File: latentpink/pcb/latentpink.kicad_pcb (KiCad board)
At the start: 8 copper layers, 145 x 139 mm, 829 parts, among them J1 CONN_SFP_HOST, J10 XILINX_JTAG, J11 FAN_01, J12 FAN_01, J13 CONN_01X05, J14 CONN_01X03, J15 CONN_01X03, J16 JUMPER_0402_SPDT, J17 JUMPER_0402_SPDT, J18 BEL_FUSE_0845-2R1T-E4, J19 BEL_FUSE_0845-2R1T-E4, J2 SFP_CAGE, J20 BEL_FUSE_0845-2R1T-E4, J21 BEL_FUSE_0845-2R1T-E4, J22 BEL_FUSE_0845-2R1T-E4, J23 PMOD_HOST, J3 XILINX_JTAG, J4 BEL_FUSE_0845-2R1T-E4, J5 0826-1G1T-23-F, J6 BARREL_JACK, J7 RJ45, J8 BEL_FUSE_0845-2R1T-E4, J9 XILINX_JTAG, M1 960-27-12-D-AB-0, M10 WEEE, M2 960-23-23-F-AB-0, M3 SCREWHOLE, M4 SCREWHOLE, M5 SCREWHOLE, M6 SCREWHOLE, M7 LONGTHING, M8 OSHW, M9 POLARITY, U1 VSC8512, U10 MYMGK1R812ERSR, U11 MYMGK00504ERSR, U12 STM32L031-QFN32, U13 MYMGK00504ERSR, U14 MYMGK00504ERSR, U15 MYMGK00504ERSR, U16 NCP45521IMNTWG-H, U17 NCP45521IMNTWG-H, U18 LP2996AMRE, U19 TPS7A2533DRVR, U2 XC7K160T-2FBG484C, U20 AT24MAC402, U21 ECX2-LMV-3CN-125.000-TR, U22 ECS-2016MVQ-250-CN, U23 ADM3101E_QFN, U24 SIT9121AI-2BF-XXS200.000000G, U25 SIT9121AI-2BF-XXS156.250000G, U26 74LVC1T45, U27 74LVC1T45, U28 IS25WP256D-JLLE, U29 DSC1123CI2-150.0000T, U3 CY7C2245KV18-450BZXI, U30 DSC1123CI2-150.0000T, U31 74LVC1T45, U32 74LVC1T45, U33 74LVC1T45, U34 74LVC1T45, U35 SIT9121AC-2B2-33E125.000000, U36 AT30TS74_UDFN, U37 AT30TS74_UDFN, U38 AT30TS74_UDFN, U39 AT30TS74_UDFN, U4 STM32H735-UFBGA176-25, U40 RCLAMP0514M, U41 RCLAMP0514M, U42 RCLAMP0514M, U43 RCLAMP0514M, U44 RCLAMP0514M, U45 RCLAMP0514M, U46 RCLAMP0514M, U47 RCLAMP0514M, U48 RCLAMP0514M, U49 RCLAMP0514M, U5 DP83867, U50 RCLAMP0514M, U51 RCLAMP0514M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

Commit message: Continued initial layout. Working on PHY decoupling caps and fanout
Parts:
- C1, C112, C264, C266, C267, C268, C270, C271, C272, C273, C274, C275, C277, C279, C280, C281, C282, C283, C286, C287, C290, C291, C294, C301, C302, C303, C308, C329, C333, C336, C337, C346, C347, C350, C351, C475, C67, C70, L4, R20, R21, R80: moved to B.Cu
- moved C100 182.3 mm to (136.0, 145.5)
- moved C107 176.0 mm to (127.8, 135.8), turned to 180 degrees
- moved C475 172.5 mm to (132.5, 138.5)
- moved C103 170.9 mm to (120.8, 145.5), turned to 180 degrees
- moved TP3 169.2 mm to (122.5, 142.0)
- moved R8 169.1 mm to (133.0, 142.0)
- moved R11 167.9 mm to (134.2, 142.5), turned to 90 degrees
- moved C112 162.2 mm to (127.8, 138.5), turned to 180 degrees
- moved TP20 147.3 mm to (111.0, 74.2)
- moved TP19 145.5 mm to (112.5, 74.2)
- moved R20 115.6 mm to (124.8, 142.0), turned to 180 degrees
- moved R21 115.5 mm to (126.0, 143.2)
- moved R36 114.3 mm to (132.5, 139.8), turned to 90 degrees
- moved C279 104.5 mm to (125.5, 89.2), turned to -90 degrees
- moved C303 104.2 mm to (117.0, 83.8)
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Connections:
- R100 pad 1: /QSGMII PHY/PHY7_LED1_N -> /QSGMII PHY/PHY6_LED1_N
- R81 pad 1: /QSGMII PHY/PHY0_LED0_N -> /QSGMII PHY/PHY1_LED0_N
- R82 pad 1: /QSGMII PHY/PHY1_LED0_N -> /QSGMII PHY/PHY0_LED0_N
- R83 pad 1: /QSGMII PHY/PHY2_LED0_N -> /QSGMII PHY/PHY3_LED0_N
- R84 pad 1: /QSGMII PHY/PHY3_LED0_N -> /QSGMII PHY/PHY2_LED0_N
- R85 pad 1: /QSGMII PHY/PHY4_LED0_N -> /QSGMII PHY/PHY5_LED0_N
- R86 pad 1: /QSGMII PHY/PHY5_LED0_N -> /QSGMII PHY/PHY4_LED0_N
- R87 pad 1: /QSGMII PHY/PHY6_LED0_N -> /QSGMII PHY/PHY7_LED0_N
- R88 pad 1: /QSGMII PHY/PHY7_LED0_N -> /QSGMII PHY/PHY6_LED0_N
- R93 pad 1: /QSGMII PHY/PHY0_LED1_N -> /QSGMII PHY/PHY1_LED1_N
- R94 pad 1: /QSGMII PHY/PHY1_LED1_N -> /QSGMII PHY/PHY0_LED1_N
- R95 pad 1: /QSGMII PHY/PHY2_LED1_N -> /QSGMII PHY/PHY3_LED1_N
- R96 pad 1: /QSGMII PHY/PHY3_LED1_N -> /QSGMII PHY/PHY2_LED1_N
- R97 pad 1: /QSGMII PHY/PHY4_LED1_N -> /QSGMII PHY/PHY5_LED1_N
- R98 pad 1: /QSGMII PHY/PHY5_LED1_N -> /QSGMII PHY/PHY4_LED1_N
- R99 pad 1: /QSGMII PHY/PHY6_LED1_N -> /QSGMII PHY/PHY7_LED1_N
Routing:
- net /GND: track 717.2 -> 865.2 mm, vias 253 -> 340
- net /12V0: track 0.00 -> 81.3 mm, vias 0 -> 10
- net /2V5: track 162.5 -> 208.7 mm, vias 37 -> 61
- net /QSGMII PHY/QSGMII Power/A2V5_VSC: track 53.7 -> 77.2 mm, vias 36 -> 46
- net /QSGMII PHY/QSGMII Power/A1V0_VSC: track 40.1 -> 60.6 mm, vias 24 -> 45
- net /QSGMII PHY/VSC_JTAG_TDO: track 60.6 -> 77.0 mm
- net /Power Supply/2V5_RAW: track 0.00 -> 7.21 mm, vias 0 -> 6
- net /QSGMII PHY/VSC_JTAG_TDI: track 60.3 -> 67.3 mm
- net /1V0: track 88.0 -> 94.7 mm, vias 81 -> 84
- net /QSGMII PHY/VSC_JTAG_TCK: track 67.8 -> 74.2 mm
- net /QSGMII PHY/VSC_CLKOUT_1: track 0.00 -> 6.21 mm
- net Net-(U1-PadW4): track 0.00 -> 5.46 mm, vias 0 -> 2
- net Net-(U1-PadV4): track 0.00 -> 5.46 mm, vias 0 -> 1
- net Net-(U1-PadT4): track 0.00 -> 5.46 mm, vias 0 -> 2
- net /QSGMII PHY/VSC_CLKOUT_0: track 0.00 -> 5.41 mm
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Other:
- board text added: "2V5_PGOOD"
- board text added: "A2V5_VSC"
- board text added: "CLKOUT0"
- board text added: "CLKOUT1"

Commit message: Lots of layout progress on bottom power/management/supervisor area
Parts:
- C110, C115, C116, C119, C121, C13, C20, C262, C284, C289, C292, C293, C313, C318, C323, C325, C331, C352, C353, C354, C466, C6, L2, L5, R106, R107, R109, R110, R111, R12, R23, R9: moved to B.Cu
- moved TP6 180.4 mm to (111.5, 25.0)
- moved C113 169.6 mm to (117.8, 132.5), turned to 90 degrees
- moved C104 169.3 mm to (118.5, 138.8), turned to -90 degrees
- moved C468 161.4 mm to (105.8, 83.3), turned to -90 degrees
- moved C467 159.7 mm to (104.8, 83.2), turned to -90 degrees
- moved U35 157.0 mm to (105.8, 80.2), turned to 180 degrees
- moved C101 156.6 mm to (115.0, 138.8), turned to 90 degrees
- moved C466 151.7 mm to (107.2, 81.2)
- moved C476 150.7 mm to (121.0, 132.5), turned to 90 degrees
- moved R9 148.6 mm to (112.5, 138.0), turned to -90 degrees
- moved C108 147.5 mm to (114.5, 132.5), turned to 90 degrees
- moved R12 146.1 mm to (112.5, 139.8), turned to 90 degrees
- moved C117 127.1 mm to (70.2, 138.0), turned to 90 degrees
- moved R109 125.1 mm to (127.0, 80.8), turned to -90 degrees
- moved D10 123.1 mm to (92.5, 141.0), turned to 180 degrees
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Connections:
- R100 pad 1: /QSGMII PHY/PHY6_LED1_N -> /QSGMII PHY/PHY7_LED1_N
- R100 pad 2: Net-(U1-PadW4) -> Net-(R100-Pad2)
- R101 pad 2: Net-(U1-PadW3) -> Net-(R101-Pad2)
- R102 pad 2: Net-(U1-PadW2) -> Net-(R102-Pad2)
- R103 pad 2: Net-(U1-PadW1) -> Net-(R103-Pad2)
- R104 pad 2: Net-(U1-PadV4) -> Net-(R104-Pad2)
- R106 pad 1: /QSGMII PHY/VSC_RST_N -> /2V5
- R106 pad 2: /2V5 -> /QSGMII PHY/VSC_RST_N
- R81 pad 1: /QSGMII PHY/PHY1_LED0_N -> /QSGMII PHY/PHY0_LED0_N
- R81 pad 2: Net-(U1-PadV3) -> Net-(U1-PadV2)
- R82 pad 1: /QSGMII PHY/PHY0_LED0_N -> /QSGMII PHY/PHY1_LED0_N
- R82 pad 2: Net-(U1-PadV2) -> Net-(U1-PadV3)
- R83 pad 1: /QSGMII PHY/PHY3_LED0_N -> /QSGMII PHY/PHY2_LED0_N
- R83 pad 2: Net-(U1-PadV1) -> Net-(R83-Pad2)
- R84 pad 1: /QSGMII PHY/PHY2_LED0_N -> /QSGMII PHY/PHY3_LED0_N
- R84 pad 2: Net-(U1-PadU4) -> Net-(R84-Pad2)
- R85 pad 1: /QSGMII PHY/PHY5_LED0_N -> /QSGMII PHY/PHY4_LED0_N
- R85 pad 2: Net-(U1-PadU3) -> Net-(R85-Pad2)
- R86 pad 1: /QSGMII PHY/PHY4_LED0_N -> /QSGMII PHY/PHY5_LED0_N
- R86 pad 2: Net-(U1-PadU2) -> Net-(R86-Pad2)
- R87 pad 1: /QSGMII PHY/PHY7_LED0_N -> /QSGMII PHY/PHY6_LED0_N
- R87 pad 2: Net-(U1-PadU1) -> Net-(R87-Pad2)
- R88 pad 1: /QSGMII PHY/PHY6_LED0_N -> /QSGMII PHY/PHY7_LED0_N
- R88 pad 2: Net-(U1-PadT4) -> Net-(R88-Pad2)
- R89 pad 2: Net-(U1-PadT3) -> Net-(R89-Pad2)
- R90 pad 2: Net-(U1-PadT2) -> Net-(R90-Pad2)
- R91 pad 2: Net-(U1-PadT1) -> Net-(R91-Pad2)
- R92 pad 2: Net-(U1-PadR4) -> Net-(R92-Pad2)
- R93 pad 1: /QSGMII PHY/PHY1_LED1_N -> /QSGMII PHY/PHY0_LED1_N
- R93 pad 2: Net-(U1-PadAA3) -> Net-(R93-Pad2)
- R94 pad 1: /QSGMII PHY/PHY0_LED1_N -> /QSGMII PHY/PHY1_LED1_N
- R94 pad 2: Net-(U1-PadAA2) -> Net-(R94-Pad2)
- R95 pad 1: /QSGMII PHY/PHY3_LED1_N -> /QSGMII PHY/PHY2_LED1_N
- R95 pad 2: Net-(U1-PadAA1) -> Net-(R95-Pad2)
- R96 pad 1: /QSGMII PHY/PHY2_LED1_N -> /QSGMII PHY/PHY3_LED1_N
- R96 pad 2: Net-(U1-PadY4) -> Net-(R96-Pad2)
- R97 pad 1: /QSGMII PHY/PHY5_LED1_N -> /QSGMII PHY/PHY4_LED1_N
- R97 pad 2: Net-(U1-PadY3) -> Net-(R97-Pad2)
- R98 pad 1: /QSGMII PHY/PHY4_LED1_N -> /QSGMII PHY/PHY5_LED1_N
- R98 pad 2: Net-(U1-PadY2) -> Net-(R98-Pad2)
- R99 pad 1: /QSGMII PHY/PHY7_LED1_N -> /QSGMII PHY/PHY6_LED1_N
- R99 pad 2: Net-(U1-PadY1) -> Net-(R99-Pad2)
- U1 pad A10: /QSGMII PHY/ETH7_D0_P -> /QSGMII PHY/ETH7_D1_P
- U1 pad A11: /QSGMII PHY/ETH7_D1_P -> /QSGMII PHY/ETH7_D0_P
- U1 pad A12: /QSGMII PHY/ETH7_D2_P -> /QSGMII PHY/ETH7_D3_P
- U1 pad A13: /QSGMII PHY/ETH7_D3_P -> /QSGMII PHY/ETH7_D2_P
- U1 pad A2: /QSGMII PHY/ETH8_D0_P -> /QSGMII PHY/ETH9_D1_P
- U1 pad A3: /QSGMII PHY/ETH8_D1_P -> /QSGMII PHY/ETH9_D0_P
- U1 pad A4: /QSGMII PHY/ETH8_D2_P -> /QSGMII PHY/ETH9_D3_P
- U1 pad A5: /QSGMII PHY/ETH8_D3_P -> /QSGMII PHY/ETH9_D2_P
- U1 pad AA1: Net-(U1-PadAA1) -> Net-(R96-Pad2)
- U1 pad AA2: Net-(U1-PadAA2) -> Net-(R93-Pad2)
- U1 pad AA3: Net-(U1-PadAA3) -> Net-(R94-Pad2)
- U1 pad B10: /QSGMII PHY/ETH7_D0_N -> /QSGMII PHY/ETH7_D1_N
- U1 pad B11: /QSGMII PHY/ETH7_D1_N -> /QSGMII PHY/ETH7_D0_N
- U1 pad B12: /QSGMII PHY/ETH7_D2_N -> /QSGMII PHY/ETH7_D3_N
- U1 pad B13: /QSGMII PHY/ETH7_D3_N -> /QSGMII PHY/ETH7_D2_N
- U1 pad B2: /QSGMII PHY/ETH8_D0_N -> /QSGMII PHY/ETH9_D1_N
- U1 pad B3: /QSGMII PHY/ETH8_D1_N -> /QSGMII PHY/ETH9_D0_N
- U1 pad B4: /QSGMII PHY/ETH8_D2_N -> /QSGMII PHY/ETH9_D3_N
- U1 pad B5: /QSGMII PHY/ETH8_D3_N -> /QSGMII PHY/ETH9_D2_N
- U1 pad C1: /QSGMII PHY/ETH9_D3_P -> /QSGMII PHY/ETH8_D2_P
- U1 pad C2: /QSGMII PHY/ETH9_D3_N -> /QSGMII PHY/ETH8_D2_N
- U1 pad D1: /QSGMII PHY/ETH9_D2_P -> /QSGMII PHY/ETH8_D3_P
- U1 pad D2: /QSGMII PHY/ETH9_D2_N -> /QSGMII PHY/ETH8_D3_N
- U1 pad E1: /QSGMII PHY/ETH9_D1_P -> /QSGMII PHY/ETH8_D0_P
- U1 pad E2: /QSGMII PHY/ETH9_D1_N -> /QSGMII PHY/ETH8_D0_N
- U1 pad F1: /QSGMII PHY/ETH9_D0_P -> /QSGMII PHY/ETH8_D1_P
- U1 pad F2: /QSGMII PHY/ETH9_D0_N -> /QSGMII PHY/ETH8_D1_N
- U1 pad G1: /QSGMII PHY/ETH10_D3_P -> /QSGMII PHY/ETH11_D2_P
- U1 pad G2: /QSGMII PHY/ETH10_D3_N -> /QSGMII PHY/ETH11_D2_N
- U1 pad H1: /QSGMII PHY/ETH10_D2_P -> /QSGMII PHY/ETH11_D3_P
- U1 pad H2: /QSGMII PHY/ETH10_D2_N -> /QSGMII PHY/ETH11_D3_N
- U1 pad J1: /QSGMII PHY/ETH10_D1_P -> /QSGMII PHY/ETH11_D0_P
- U1 pad J2: /QSGMII PHY/ETH10_D1_N -> /QSGMII PHY/ETH11_D0_N
- U1 pad K1: /QSGMII PHY/ETH10_D0_P -> /QSGMII PHY/ETH11_D1_P
- U1 pad K2: /QSGMII PHY/ETH10_D0_N -> /QSGMII PHY/ETH11_D1_N
- U1 pad L1: /QSGMII PHY/ETH11_D3_P -> /QSGMII PHY/ETH10_D3_P
- U1 pad L2: /QSGMII PHY/ETH11_D3_N -> /QSGMII PHY/ETH10_D3_N
- U1 pad M1: /QSGMII PHY/ETH11_D2_P -> /QSGMII PHY/ETH10_D2_P
- U1 pad M2: /QSGMII PHY/ETH11_D2_N -> /QSGMII PHY/ETH10_D2_N
- U1 pad N1: /QSGMII PHY/ETH11_D1_P -> /QSGMII PHY/ETH10_D1_P
- U1 pad N2: /QSGMII PHY/ETH11_D1_N -> /QSGMII PHY/ETH10_D1_N
- U1 pad P1: /QSGMII PHY/ETH11_D0_P -> /QSGMII PHY/ETH10_D0_P
- U1 pad P2: /QSGMII PHY/ETH11_D0_N -> /QSGMII PHY/ETH10_D0_N
- U1 pad R4: Net-(U1-PadR4) -> Net-(R91-Pad2)
- U1 pad T1: Net-(U1-PadT1) -> Net-(R92-Pad2)
- U1 pad T2: Net-(U1-PadT2) -> Net-(R89-Pad2)
- U1 pad T3: Net-(U1-PadT3) -> Net-(R90-Pad2)
- U1 pad T4: Net-(U1-PadT4) -> Net-(R87-Pad2)
- U1 pad U1: Net-(U1-PadU1) -> Net-(R88-Pad2)
- U1 pad U2: Net-(U1-PadU2) -> Net-(R85-Pad2)
- U1 pad U3: Net-(U1-PadU3) -> Net-(R86-Pad2)
- U1 pad U4: Net-(U1-PadU4) -> Net-(R83-Pad2)
- U1 pad V1: Net-(U1-PadV1) -> Net-(R84-Pad2)
- U1 pad V4: Net-(U1-PadV4) -> Net-(R103-Pad2)
- U1 pad W1: Net-(U1-PadW1) -> Net-(R104-Pad2)
- U1 pad W2: Net-(U1-PadW2) -> Net-(R101-Pad2)
- U1 pad W3: Net-(U1-PadW3) -> Net-(R102-Pad2)
- U1 pad W4: Net-(U1-PadW4) -> Net-(R99-Pad2)
- U1 pad Y1: Net-(U1-PadY1) -> Net-(R100-Pad2)
- U1 pad Y2: Net-(U1-PadY2) -> Net-(R97-Pad2)
- U1 pad Y3: Net-(U1-PadY3) -> Net-(R98-Pad2)
- U1 pad Y4: Net-(U1-PadY4) -> Net-(R95-Pad2)
- U12 pad 2: /Power Supply/VTT_EN -> /Power Supply/ALL_OK
- U12 pad 21: /Power Supply/PWR_FAIL -> /Power Supply/VTT_EN
- U12 pad 3: /Power Supply/SUPER_GPIO -> /Power Supply/PWR_FAIL
- U12 pad 32: /Power Supply/ALL_OK -> /Power Supply/SUPER_GPIO
- U12 pad 6: /Power Supply/3V3_EN -> /Power Supply/PWR_OK
- U12 pad 7: /Power Supply/PWR_OK -> /Power Supply/3V3_EN
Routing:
- net /GND: track 865.2 -> 1372.7 mm, vias 340 -> 480
- net /3V3: track 318.6 -> 411.1 mm, vias 0 -> 9
- net /2V5: track 208.7 -> 284.6 mm, vias 61 -> 76
- net /QSGMII PHY/ETH8_D1_P: track 0.00 -> 55.9 mm, vias 0 -> 2
- net /QSGMII PHY/ETH8_D1_N: track 0.00 -> 55.8 mm, vias 0 -> 2
- net /QSGMII PHY/VSC_RST_N: track 0.00 -> 54.4 mm, vias 0 -> 2
- net /3V3_SB: track 0.00 -> 53.4 mm, vias 0 -> 10
- net /QSGMII PHY/VSC_POWERDOWN: track 0.00 -> 52.8 mm, vias 0 -> 2
- net /QSGMII PHY/ETH8_D3_N: track 0.00 -> 52.5 mm, vias 0 -> 2
- net /QSGMII PHY/ETH8_D3_P: track 0.00 -> 52.4 mm, vias 0 -> 2
- net Net-(R90-Pad2): track 0.00 -> 51.7 mm, vias 0 -> 2
- net /QSGMII PHY/ETH8_D2_N: track 0.00 -> 51.2 mm, vias 0 -> 2
- net /QSGMII PHY/ETH8_D2_P: track 0.00 -> 51.2 mm, vias 0 -> 2
- net /QSGMII PHY/ETH8_D0_N: track 0.00 -> 50.5 mm, vias 0 -> 2
- net /QSGMII PHY/ETH8_D0_P: track 0.00 -> 50.5 mm, vias 0 -> 2
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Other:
- board text added: "2V5_ PGOOD"
- board text added: "3V3_SB OK"
- board text added: "3V3_SB_ PGOOD"
- board text added: "A1V0_ SERDES1"
- board text added: "A1V0_ SERDES2"
- board text added: "A2V5_ VSC"
- board text added: "ALL OK"
- board text added: "BL"
- board text added: "MCU BOOT"
- board text added: "MCU GPIO[0]"
- board text added: "MCU GPIO[1]"
- board text added: "MCU GPIO[2]"
- board text added: "MCU GPIO[3]"
- board text added: "NORM"
- board text added: "PWR FAIL"
- board text added: "PWR OK"
- board text added: "SUPER GPIO"
- board text removed: "2V5_PGOOD"
- board text removed: "A2V5_VSC"

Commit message: Progress on management / power region at south
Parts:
- C263, C265, L3, R48: moved to B.Cu
- moved D12 115.5 mm to (92.5, 133.5), turned to 180 degrees
- moved D15 115.1 mm to (92.5, 137.2), turned to 180 degrees
- moved D13 114.8 mm to (92.5, 134.8), turned to 180 degrees
- moved D14 111.5 mm to (92.5, 136.0), turned to 180 degrees
- moved R161 109.8 mm to (90.2, 134.8)
- moved R163 109.3 mm to (90.2, 137.2)
- moved R162 109.1 mm to (90.2, 136.0)
- moved R160 108.4 mm to (90.2, 133.5)
- moved C265 88.1 mm to (117.8, 107.5), turned to 180 degrees
- moved TP37 87.5 mm to (121.5, 122.0), turned to 180 degrees
- moved R48 86.5 mm to (107.2, 145.0), turned to 180 degrees
- moved L3 83.2 mm to (118.0, 110.8), turned to -90 degrees
- moved C263 78.4 mm to (118.0, 114.5), turned to -90 degrees
- moved C458 53.1 mm to (190.0, 137.2)
- moved C459 53.1 mm to (190.0, 142.8)
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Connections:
- D16 pad 1: Net-(D16-Pad1) -> /GND
- D17 pad 1: Net-(D16-Pad1) -> /GND
- J2 pad 1: /GND -> /CHGND
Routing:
- net /CHGND: track 308.7 -> 546.7 mm
- net /1V8: track 0.00 -> 74.9 mm
- net /Power Supply/2V5_PGOOD: track 2.75 -> 53.1 mm, vias 1 -> 4
- net /Power Supply/2V5_EN: track 0.00 -> 48.0 mm, vias 1 -> 3
- net /3V3_SB: track 53.4 -> 85.7 mm, vias 10 -> 11
- net /FPGA/FPGA_JTAG_TDI: track 0.00 -> 31.4 mm
- net /FPGA/FPGA_JTAG_TDO: track 0.00 -> 30.8 mm
- net /QSGMII PHY/QSGMII Power/A1V0_VSC: track 60.6 -> 90.9 mm, vias 45 -> 52
- net /GND: track 1372.7 -> 1342.4 mm, vias 480 -> 501
- net /FPGA/FPGA_JTAG_TCK: track 0.00 -> 29.8 mm
- net /FPGA/FPGA_JTAG_TMS: track 0.00 -> 29.0 mm
- net /Power Supply/3V3_PGOOD: track 0.00 -> 27.8 mm, vias 1 -> 2
- net /Management/MCU_JTAG_TDI: track 0.00 -> 24.1 mm
- net /Management/MCU_JTAG_TDO: track 0.00 -> 23.3 mm
- net /Management/MCU_JTAG_TCK: track 0.00 -> 21.6 mm
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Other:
- board text added: "A1V0_ VSC"
- board text added: "FPGA GPIO[0]"
- board text added: "FPGA GPIO[1]"
- board text added: "FPGA GPIO[2]"
- board text added: "FPGA GPIO[3]"
- board text removed: "VSC8512 decoupling"

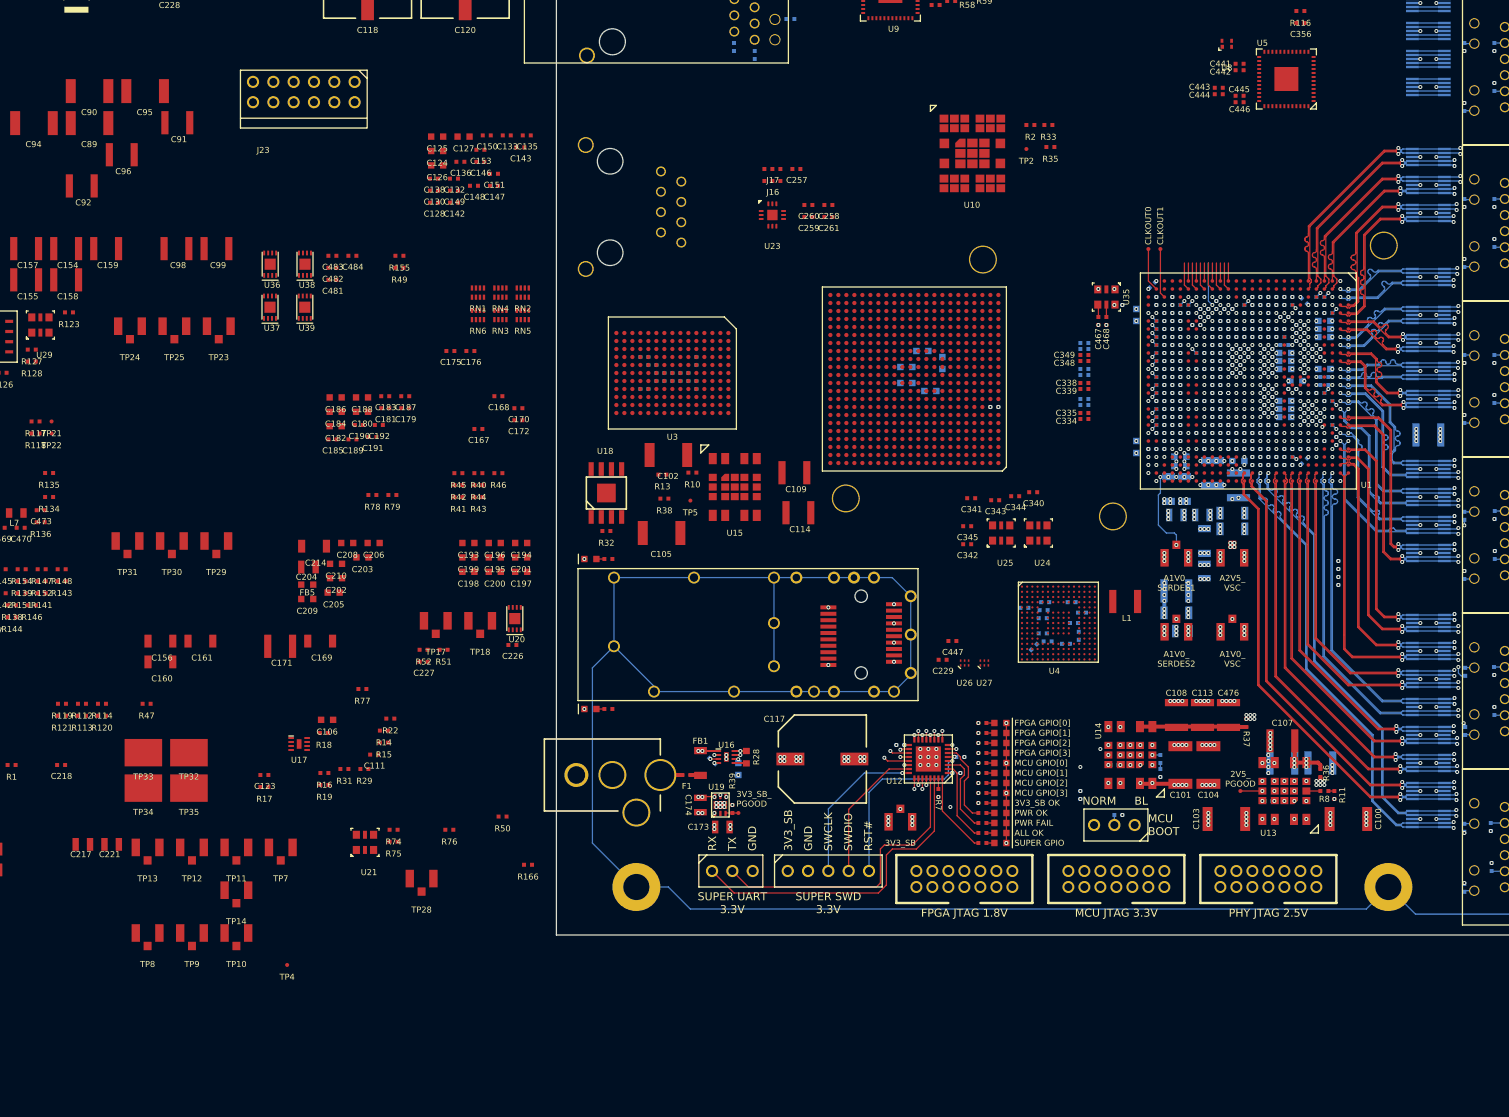
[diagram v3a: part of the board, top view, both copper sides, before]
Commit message: Continued work on management MCU area
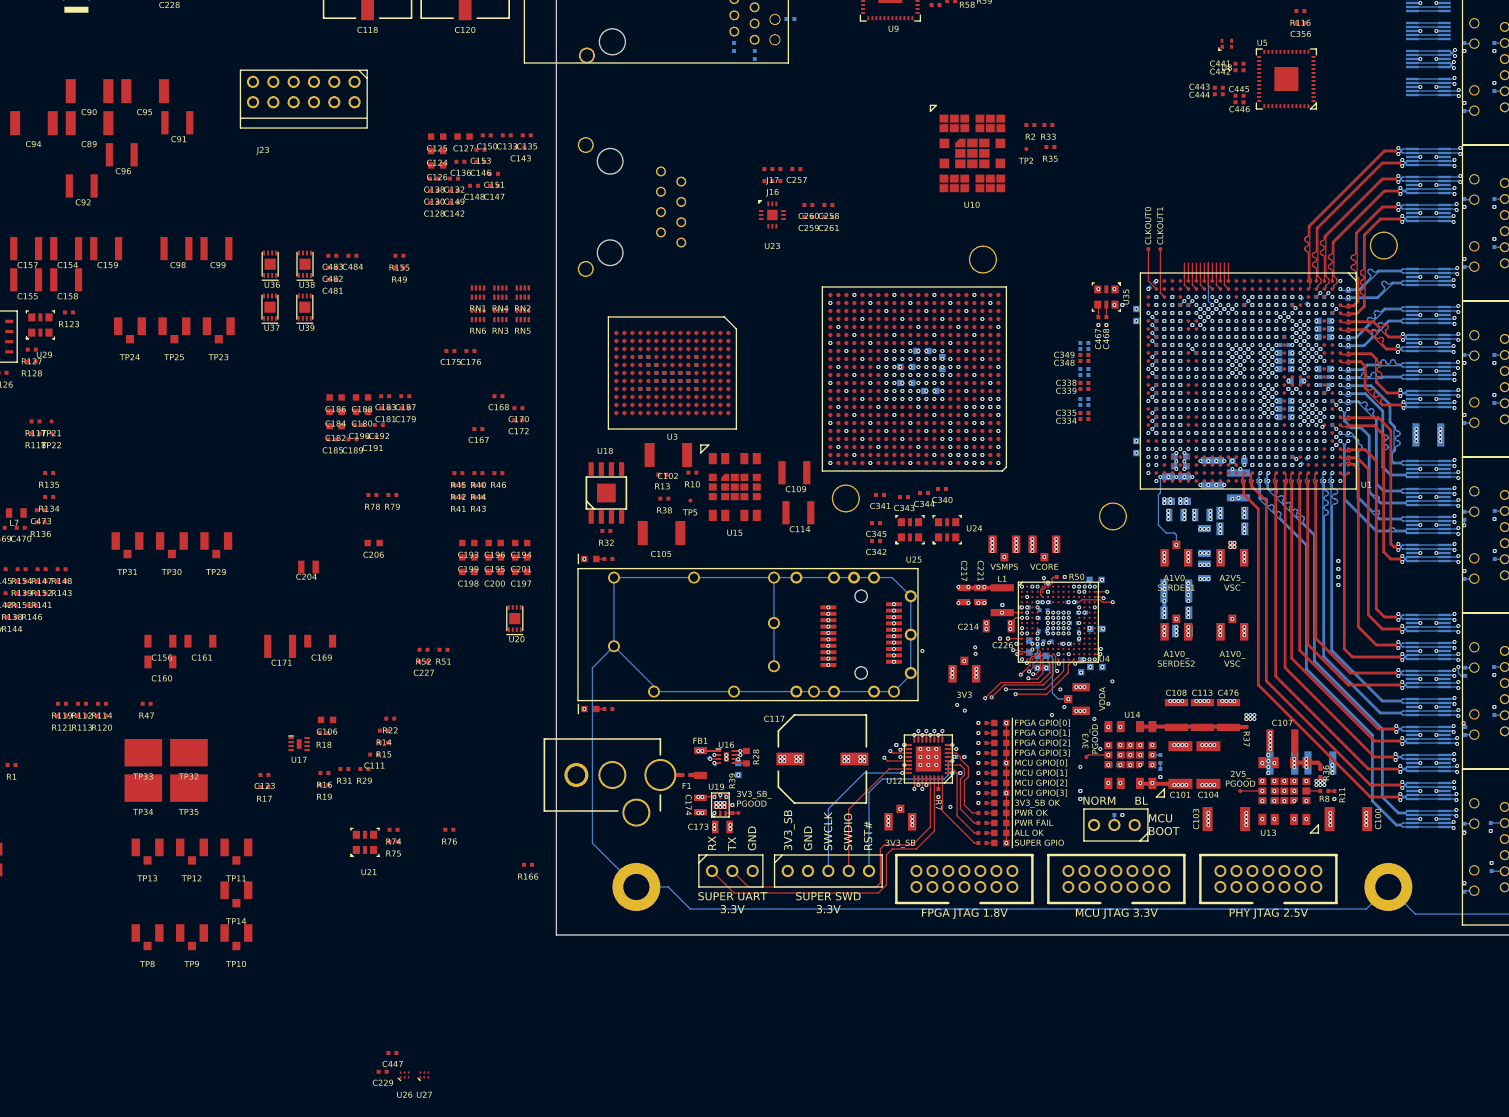
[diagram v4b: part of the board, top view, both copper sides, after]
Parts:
- C202, C203, C205, C208, C209, C210, C218, FB5, R77: moved to B.Cu
- moved C218 119.3 mm to (92.8, 119.2), turned to 90 degrees
- moved C217 114.5 mm to (88.0, 117.5), turned to -90 degrees
- moved C221 113.0 mm to (90.0, 117.5), turned to -90 degrees
- moved TP4 103.2 mm to (103.2, 137.8)
- moved C209 97.1 mm to (102.6, 126.4), turned to -90 degrees
- moved C205 95.3 mm to (104.4, 115.6)
- moved C208 94.3 mm to (104.5, 121.8), turned to 180 degrees
- moved C203 92.8 mm to (104.5, 126.5)
- moved FB5 91.8 mm to (97.2, 125.8), turned to 90 degrees
- moved C210 89.6 mm to (98.2, 125.8), turned to -90 degrees
- moved TP7 88.2 mm to (88.0, 127.2), turned to 180 degrees
- moved C202 87.1 mm to (96.1, 124.0), turned to -90 degrees
- moved C229 86.9 mm to (15.3, 177.1)
- moved C447 86.9 mm to (16.5, 174.8)
- moved U26 86.9 mm to (18.0, 177.5)
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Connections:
- U4 pad B11: /Management/MCU_LED0 -> unconnected-(U4-PadB11)
- U4 pad C1: /Management/MCU_LED1 -> unconnected-(U4-PadC1)
- U4 pad D1: /Management/MCU_LED3 -> unconnected-(U4-PadD1)
- U4 pad D2: /Management/MCU_LED2 -> unconnected-(U4-PadD2)
- U4 pad K14: /Management/MCU_HEARTBEAT -> unconnected-(U4-PadK14)
- U4 pad K15: /Management/HARD_RESET_REQ -> unconnected-(U4-PadK15)
- U4 pad M11: /QSGMII PHY/SFP_TX_FAULT -> unconnected-(U4-PadM11)
- U4 pad N15: unconnected-(U4-PadN15) -> /QSGMII PHY/SFP_TX_FAULT
- U4 pad P10: unconnected-(U4-PadP10) -> /Management/HARD_RESET_REQ
- U4 pad P8: unconnected-(U4-PadP8) -> /Management/MCU_HEARTBEAT
- U4 pad R11: unconnected-(U4-PadR11) -> /Management/MCU_LED3
- U4 pad R6: unconnected-(U4-PadR6) -> /Management/MCU_LED0
- U4 pad R7: unconnected-(U4-PadR7) -> /Management/MCU_LED1
- U4 pad R9: unconnected-(U4-PadR9) -> /Management/MCU_LED2
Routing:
- net /GND: track 1342.4 -> 1676.2 mm, vias 501 -> 678
- net /3V3: track 411.1 -> 466.1 mm, vias 9 -> 35
- net /Management/VSMPS: track 0.00 -> 50.2 mm, vias 0 -> 10
- net /QSGMII PHY/SFP_TX_FAULT: track 0.00 -> 41.8 mm, vias 0 -> 2
- net /QSGMII PHY/SFP_TX_DISABLE: track 0.00 -> 41.4 mm, vias 0 -> 2
- net /QSGMII PHY/SFP_I2C_SDA: track 0.00 -> 40.7 mm, vias 0 -> 2
- net /QSGMII PHY/SFP_I2C_SCL: track 0.00 -> 37.7 mm, vias 0 -> 2
- net /QSGMII PHY/SFP_RX_P: track 0.00 -> 34.3 mm, vias 0 -> 2
- net /QSGMII PHY/SFP_RX_N: track 0.00 -> 34.3 mm, vias 0 -> 2
- net /QSGMII PHY/SFP_MOD_ABS: track 0.00 -> 32.4 mm, vias 0 -> 2
- net /QSGMII PHY/SFP_RX_LOS: track 0.00 -> 31.9 mm, vias 0 -> 2
- net /Management/MCU_HEARTBEAT: track 1.35 -> 31.8 mm, vias 1 -> 3
- net /Management/HARD_RESET_REQ: track 0.85 -> 30.1 mm, vias 1 -> 3
- net /QSGMII PHY/SFP_RS1: track 0.00 -> 26.9 mm, vias 0 -> 2
- net /Management/MCU_BOOT0: track 13.4 -> 40.2 mm, vias 1 -> 4
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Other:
- board text added: "3V3"
- board text added: "3V3_ PGOOD"
- board text added: "VCORE"
- board text added: "VDDA"
- board text added: "VSMPS"
